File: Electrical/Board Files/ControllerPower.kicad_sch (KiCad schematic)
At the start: 35 parts

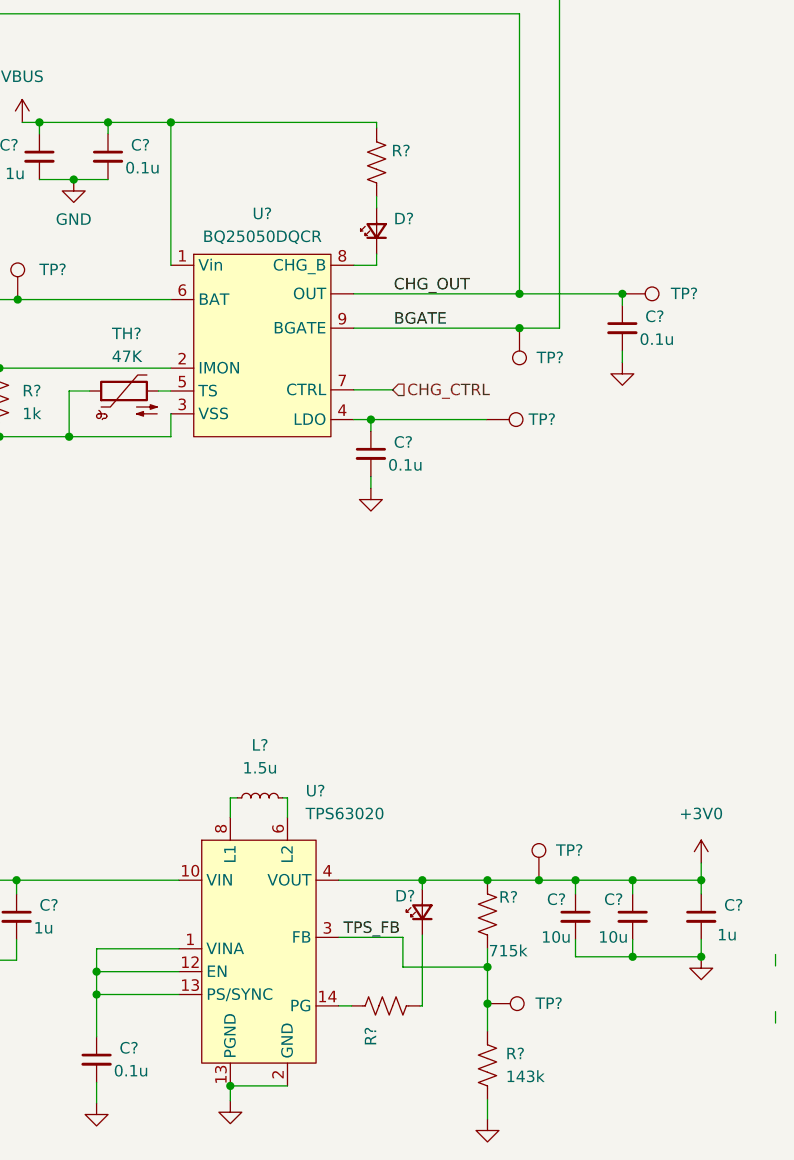
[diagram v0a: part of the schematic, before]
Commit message: Adding new block diagram
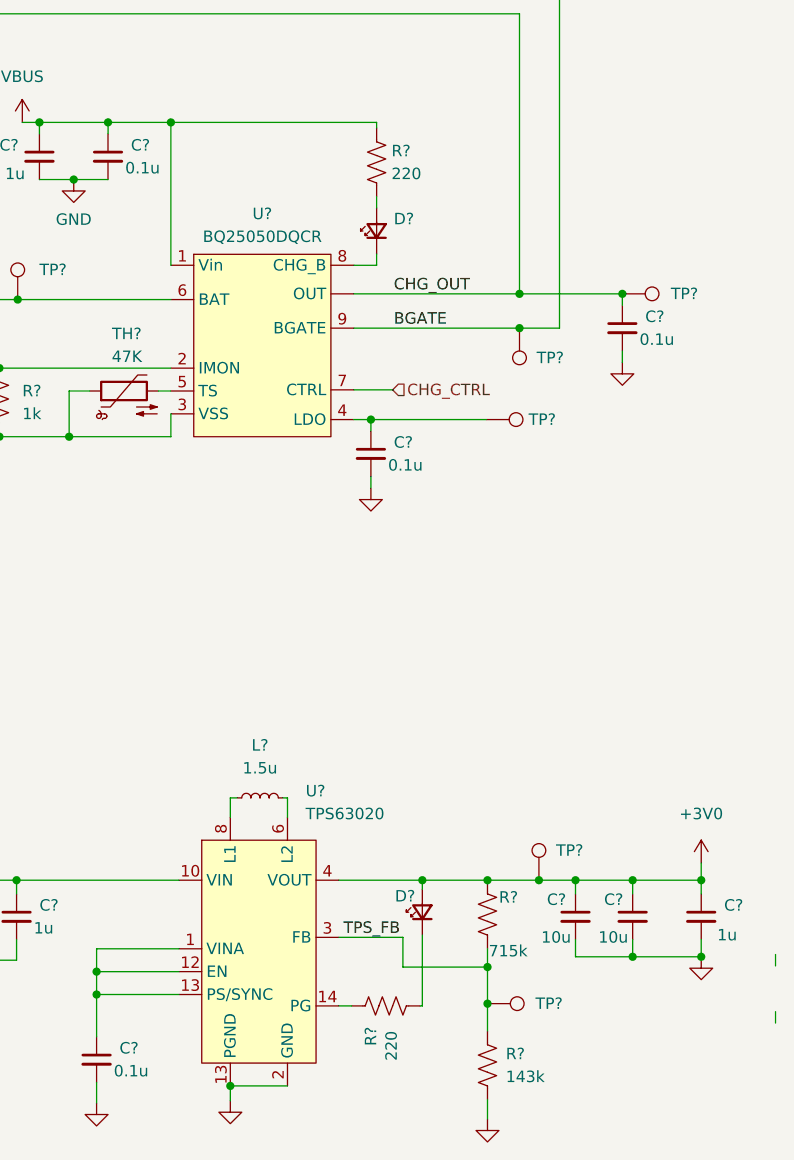
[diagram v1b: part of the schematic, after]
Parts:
- J?: value (none) -> Conn_01x02_Female
- R? (x2): value (none) -> 220
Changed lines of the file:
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@@
       (effects (font (size 1.27 1.27)) (justify left))
     )
-    (property "Value" "" (id 1) (at 111.76 52.0699 0)
+    (property "Value" "220" (id 1) (at 111.76 52.0699 0)
       (effects (font (size 1.27 1.27)) (justify left))
     )
@@
       (effects (font (size 1.27 1.27)) (justify left))
     )
-    (property "Value" "" (id 1) (at 111.76 150.622 0)
+    (property "Value" "220" (id 1) (at 111.76 150.622 0)
       (effects (font (size 1.27 1.27)) (justify left))
     )
@@
     (in_bom yes) (on_board yes) (fields_autoplaced)
     (property "Reference" "J?" (id 0) (at 18.415 63.5 0))
-    (property "Value" "" (id 1) (at 18.415 63.5 0)
-      (effects (font (size 1.27 1.27)) hide)
-    )
+    (property "Value" "Conn_01x02_Female" (id 1) (at 18.415 63.5 0)
+      (effects (font (size 1.27 1.27)) hide)
+    )

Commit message: Updating Files
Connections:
- net CHG_OUT: now also Q?.2 (S); no longer Q?.3 (D)
- net VBAT: now also Q?.3 (D); no longer Q?.2 (S)
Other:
- moved on the sheet: Q?
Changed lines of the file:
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@@
   (junction (at 56.134 130.556) (diameter 0) (color 0 0 0 0)
   )
-  (junction (at 56.769 66.04) (diameter 0) (color 0 0 0 0)
-  )
   (junction (at 59.817 84.455) (diameter 0) (color 0 0 0 0)
   )
@@
   (junction (at 80.264 46.355) (diameter 0) (color 0 0 0 0)
   )
+  (junction (at 56.007 66.04) (diameter 0) (color 0 0 0 0)
+  )
   (junction (at 115.189 130.556) (diameter 0) (color 0 0 0 0)
   )
@@
     (stroke (width 0) (type default) (color 0 0 0 0))
   )
-  (wire (pts (xy 49.149 56.515) (xy 49.149 31.115))
-    (stroke (width 0) (type default) (color 0 0 0 0))
-  )
   (wire (pts (xy 56.134 139.446) (xy 62.484 139.446))
     (stroke (width 0) (type default) (color 0 0 0 0))
@@
     (stroke (width 0) (type default) (color 0 0 0 0))
   )
-  (wire (pts (xy 52.324 66.04) (xy 56.769 66.04))
+  (wire (pts (xy 45.974 51.308) (xy 48.387 51.308))
     (stroke (width 0) (type default) (color 0 0 0 0))
   )
@@
     (stroke (width 0) (type default) (color 0 0 0 0))
   )
-  (wire (pts (xy 125.984 34.29) (xy 56.769 34.29))
+  (wire (pts (xy 56.007 34.29) (xy 125.984 34.29))
     (stroke (width 0) (type default) (color 0 0 0 0))
   )
@@
     (stroke (width 0) (type default) (color 0 0 0 0))
   )
-  (wire (pts (xy 49.149 31.115) (xy 130.429 31.115))
+  (wire (pts (xy 45.974 31.115) (xy 130.429 31.115))
     (stroke (width 0) (type default) (color 0 0 0 0))
   )
@@
     (stroke (width 0) (type default) (color 0 0 0 0))
   )
+  (wire (pts (xy 56.007 66.04) (xy 70.231 66.04))
+    (stroke (width 0) (type default) (color 0 0 0 0))
+  )
   (wire (pts (xy 78.994 140.716) (xy 78.994 143.256))
     (stroke (width 0) (type default) (color 0 0 0 0))
@@
     (stroke (width 0) (type default) (color 0 0 0 0))
   )
+  (wire (pts (xy 45.974 31.115) (xy 45.974 51.308))
+    (stroke (width 0) (type default) (color 0 0 0 0))
+  )
   (wire (pts (xy 22.86 66.04) (xy 32.004 66.04))
     (stroke (width 0) (type default) (color 0 0 0 0))
@@
     (stroke (width 0) (type default) (color 0 0 0 0))
   )
+  (wire (pts (xy 56.007 56.388) (xy 56.007 66.04))
+    (stroke (width 0) (type default) (color 0 0 0 0))
+  )
   (wire (pts (xy 93.853 121.412) (xy 94.615 121.412))
     (stroke (width 0) (type default) (color 0 0 0 0))
@@
     (stroke (width 0) (type default) (color 0 0 0 0))
   )
-  (wire (pts (xy 56.769 61.595) (xy 56.769 66.04))
-    (stroke (width 0) (type default) (color 0 0 0 0))
-  )
-  (wire (pts (xy 56.769 66.04) (xy 70.231 66.04))
+  (wire (pts (xy 52.324 66.04) (xy 56.007 66.04))
     (stroke (width 0) (type default) (color 0 0 0 0))
   )
@@
     (stroke (width 0) (type default) (color 0 0 0 0))
   )
+  (wire (pts (xy 56.007 46.228) (xy 56.007 34.29))
+    (stroke (width 0) (type default) (color 0 0 0 0))
+  )
   (wire (pts (xy 78.994 138.176) (xy 78.994 140.716))
-    (stroke (width 0) (type default) (color 0 0 0 0))
-  )
-  (wire (pts (xy 56.769 34.29) (xy 56.769 51.435))
     (stroke (width 0) (type default) (color 0 0 0 0))
   )
@@
     (effects (font (size 1.27 1.27)) (justify left bottom))
   )
+  (label "VBAT" (at 36.576 66.04 0)
+    (effects (font (size 1.27 1.27)) (justify left bottom))
+  )
   (label "CHG_OUT" (at 112.014 65.405 0)
     (effects (font (size 1.27 1.27)) (justify left bottom))
@@
     (pin "2")
   )
-  (symbol (lib_id "Device:Q_PMOS_GSD") (at 54.229 56.515 0) (unit 1)
+  (symbol (lib_id "Device:Q_PMOS_GSD") (at 53.467 51.308 0) (mirror x) (unit 1)
     (in_bom yes) (on_board yes) (fields_autoplaced)
-    (property "Reference" "Q?" (id 0) (at 59.69 55.2449 0)
-      (effects (font (size 1.27 1.27)) (justify left))
-    )
-    (property "Value" "PJA3411" (id 1) (at 59.69 57.7849 0)
-      (effects (font (size 1.27 1.27)) (justify left))
-    )
-    (property "Footprint" "" (id 2) (at 59.309 53.975 0)
-      (effects (font (size 1.27 1.27)) hide)
-    )
-    (property "Datasheet" "https://www.panjit.com.tw/upload/datasheet/PJA3411-AU.pdf" (id 3) (at 54.229 56.515 0)
-      (effects (font (size 1.27 1.27)) hide)
-    )
+    (property "Reference" "Q?" (id 0) (at 59.309 50.0379 0)
+      (effects (font (size 1.27 1.27)) (justify left))
+    )
+    (property "Value" "PJA3411" (id 1) (at 59.309 52.5779 0)
+      (effects (font (size 1.27 1.27)) (justify left))
+    )
+    (property "Footprint" "" (id 2) (at 58.547 53.848 0)
+      (effects (font (size 1.27 1.27)) hide)
+    )
+    (property "Datasheet" "https://www.panjit.com.tw/upload/datasheet/PJA3411-AU.pdf" (id 3) (at 53.467 51.308 0)
+      (effects (font (size 1.27 1.27)) hide)
+    )

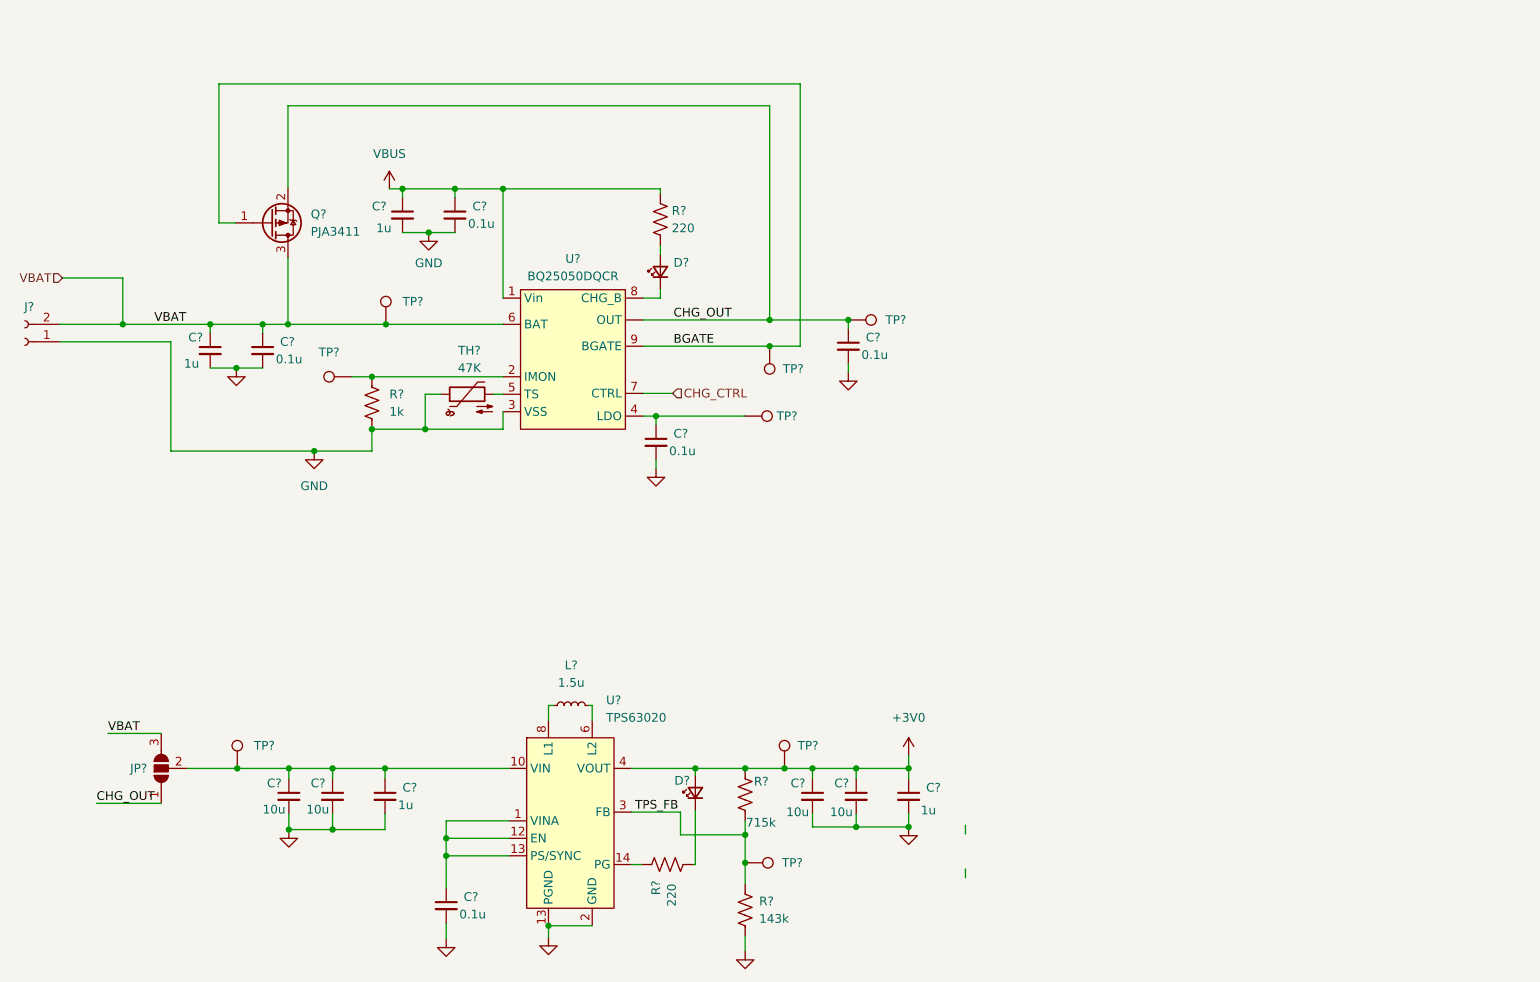
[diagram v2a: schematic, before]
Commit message: Updating for 3v3 operation
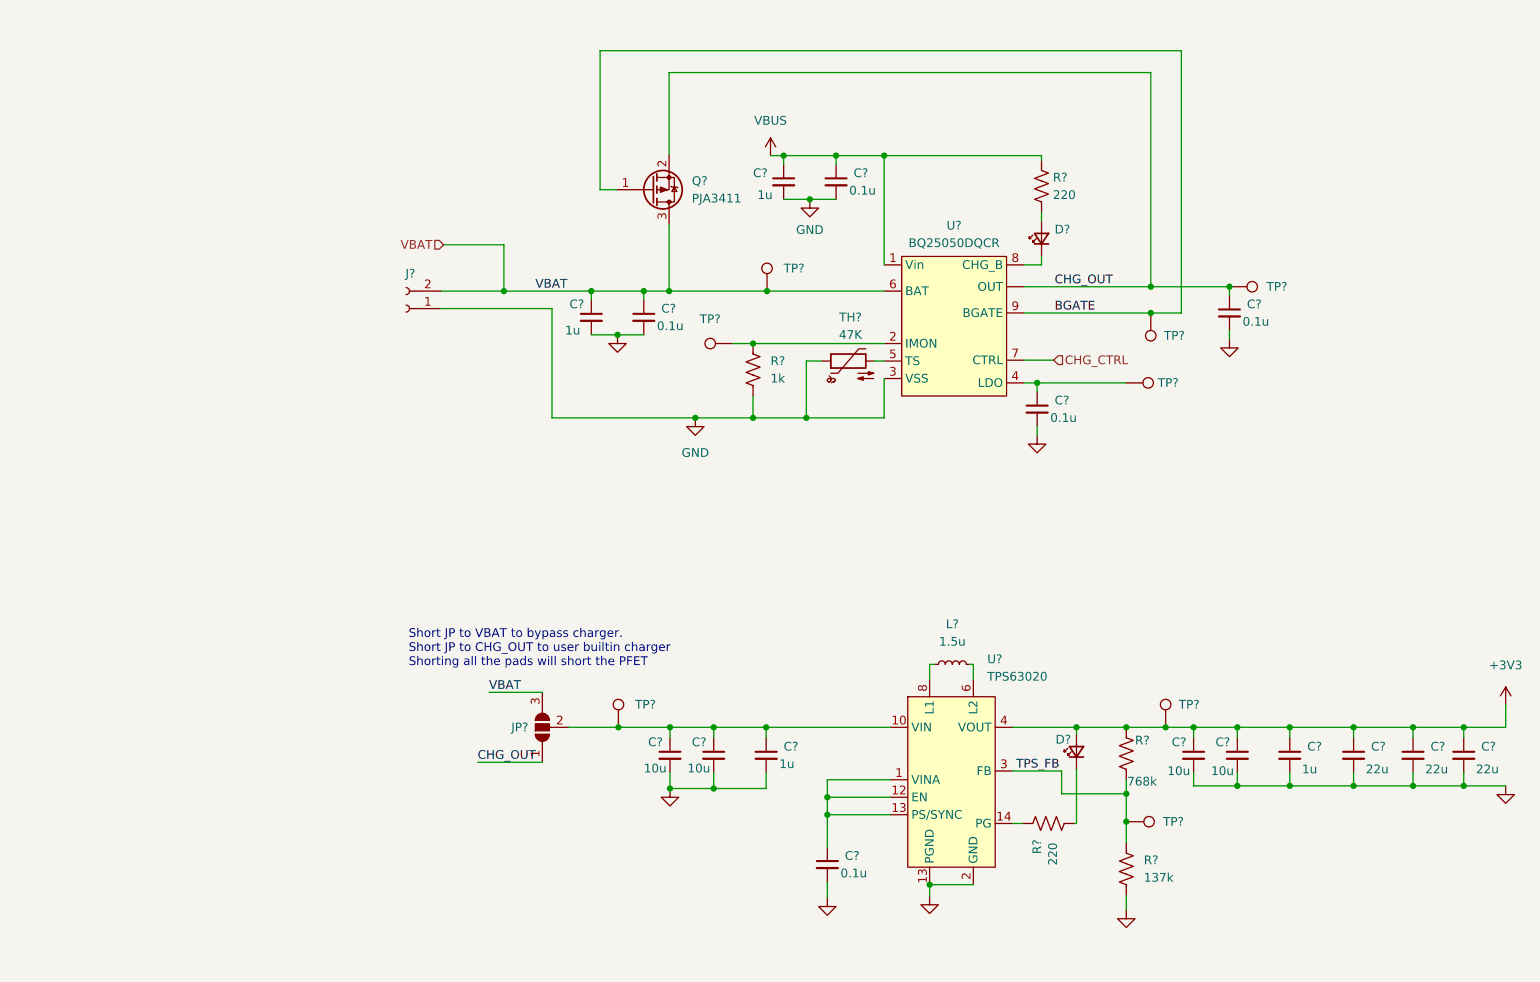
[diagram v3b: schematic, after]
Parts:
- added C? (x3): 22u, symbol Device:C_Small
- R?: value 143k -> 137k
- R?: value 715k -> 768k
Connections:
- net GND: now also C?.2, C?.2, C?.2
- net +3V0 renamed +3V3
- net +3V3: now also C?.1, C?.1, C?.1
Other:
- note added: "Short JP to VBAT to bypass charger. Short JP to CHG_OUT to user builtin charger Shorting all the pads will short the PFET"
- moved on the sheet: C?, D?, J?, JP?, L?, Q?, R?, TH?, TP?, U?

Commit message: Adding power dissipation notes. Removing WS2821B since they won't work with a 3v3 supply
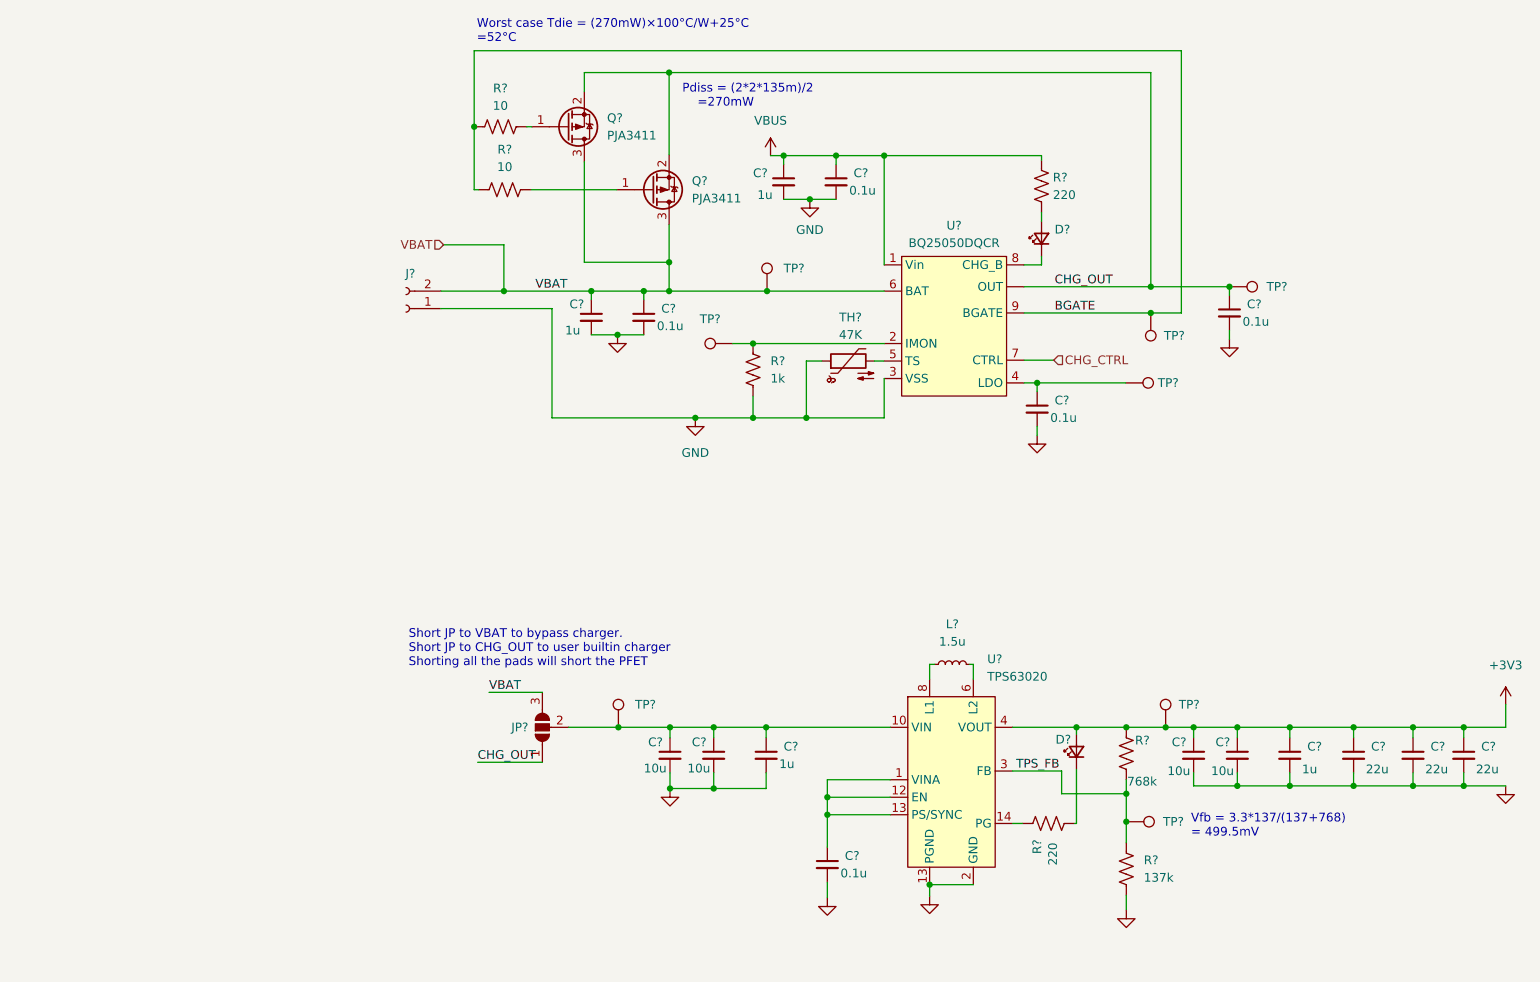
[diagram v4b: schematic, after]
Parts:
- added Q?: PJA3411, symbol Device:Q_PMOS_GSD
- added R? (x2): 10, symbol Device:R_US
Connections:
- net BGATE: now also R?.1, R?.1; no longer Q?.1 (G)
- net CHG_OUT: now also Q?.2 (S)
- net VBAT: now also Q?.3 (D)
- new net: Q?.1 (G), R?.2 (x2)
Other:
- note added: "Pdiss = (2*2*135m)/2 =270mW"
- note added: "Vfb = 3.3*137/(137+768) = 499.5mV"
- note added: "Worst case Tdie = (270mW)×100°C/W+25°C =52°C"

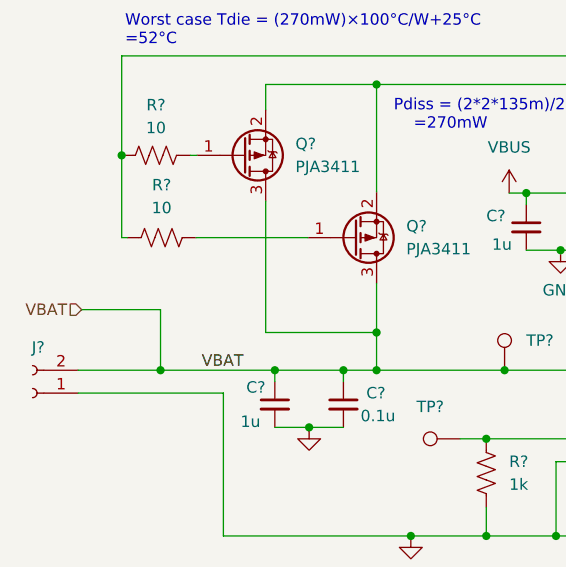
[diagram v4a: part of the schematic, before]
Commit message: Added buzz and vibe, moved SPI, added 2 LEDs
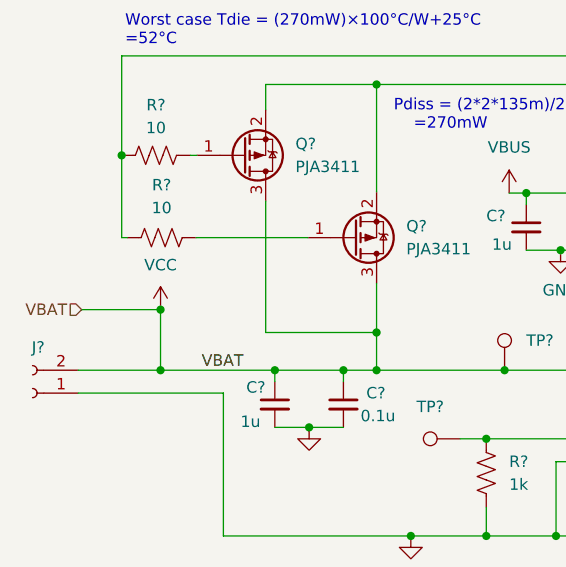
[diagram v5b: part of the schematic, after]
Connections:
- net VBAT renamed VCC
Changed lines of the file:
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@@
   (junction (at 170.561 124.587) (diameter 0) (color 0 0 0 0)
+  )
+  (junction (at 87.376 54.483) (diameter 0) (color 0 0 0 0)
   )
   (junction (at 111.506 133.477) (diameter 0) (color 0 0 0 0)
@@
       (effects (font (size 1.27 1.27)) hide)
     )
+    (pin "1")
+  )
+  (symbol (lib_id "power:VCC") (at 87.376 54.483 0) (unit 1)
+    (in_bom yes) (on_board yes) (fields_autoplaced)
+    (property "Reference" "#PWR?" (id 0) (at 87.376 58.293 0)
+      (effects (font (size 1.27 1.27)) hide)
+    )
+    (property "Value" "VCC" (id 1) (at 87.376 49.53 0))
+    (property "Footprint" "" (id 2) (at 87.376 54.483 0)
+      (effects (font (size 1.27 1.27)) hide)
+    )
+    (property "Datasheet" "" (id 3) (at 87.376 54.483 0)
+      (effects (font (size 1.27 1.27)) hide)
+    )
